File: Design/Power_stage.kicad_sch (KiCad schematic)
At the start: 4 parts, among them U3 CRE1S0505S3C, U6 CRE1S0505S3C

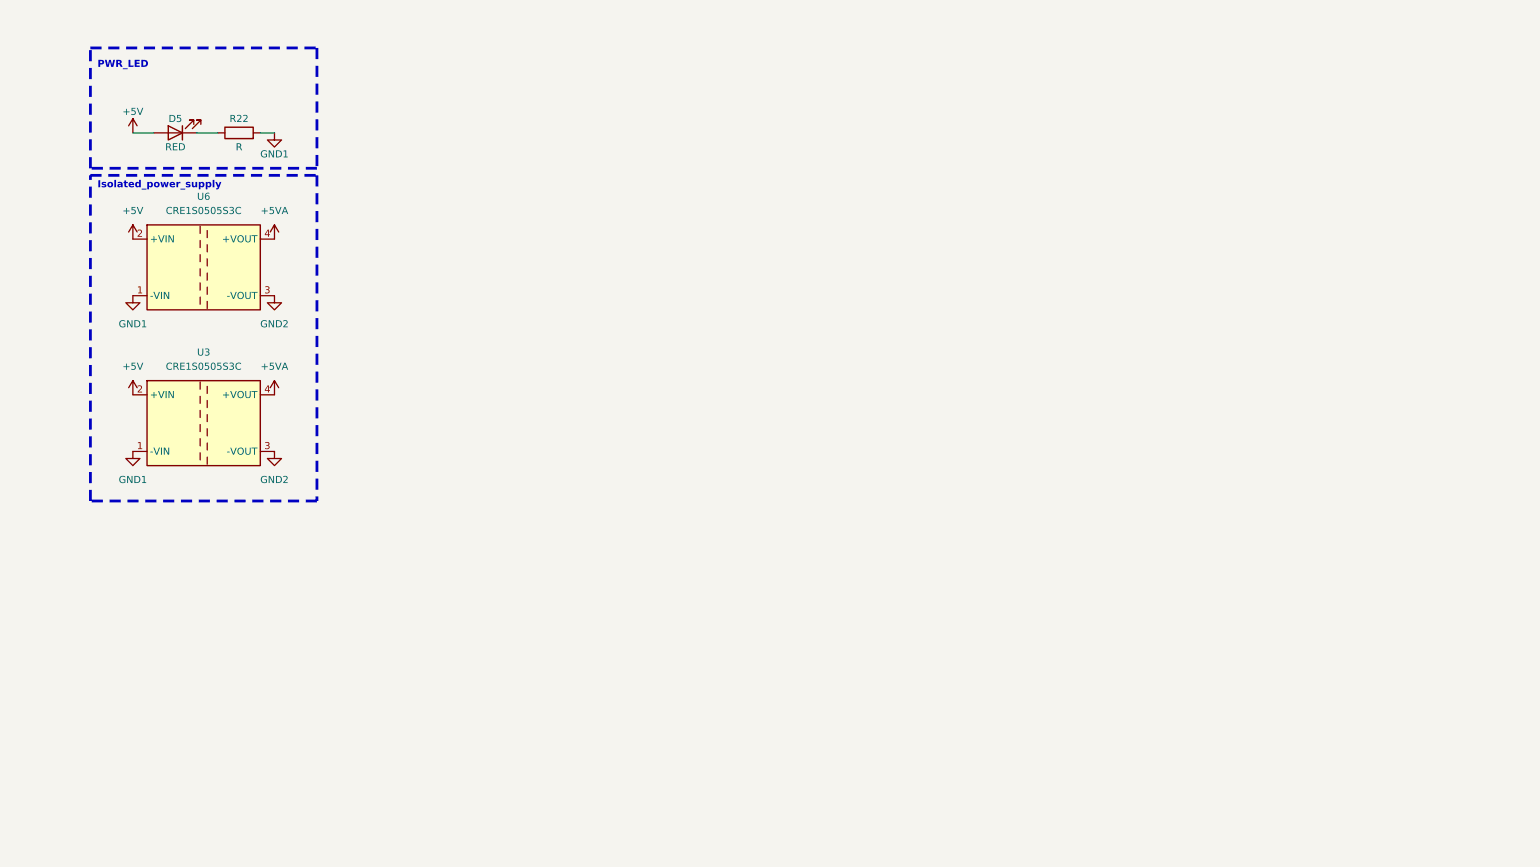
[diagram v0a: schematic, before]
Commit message: Setup Power supply
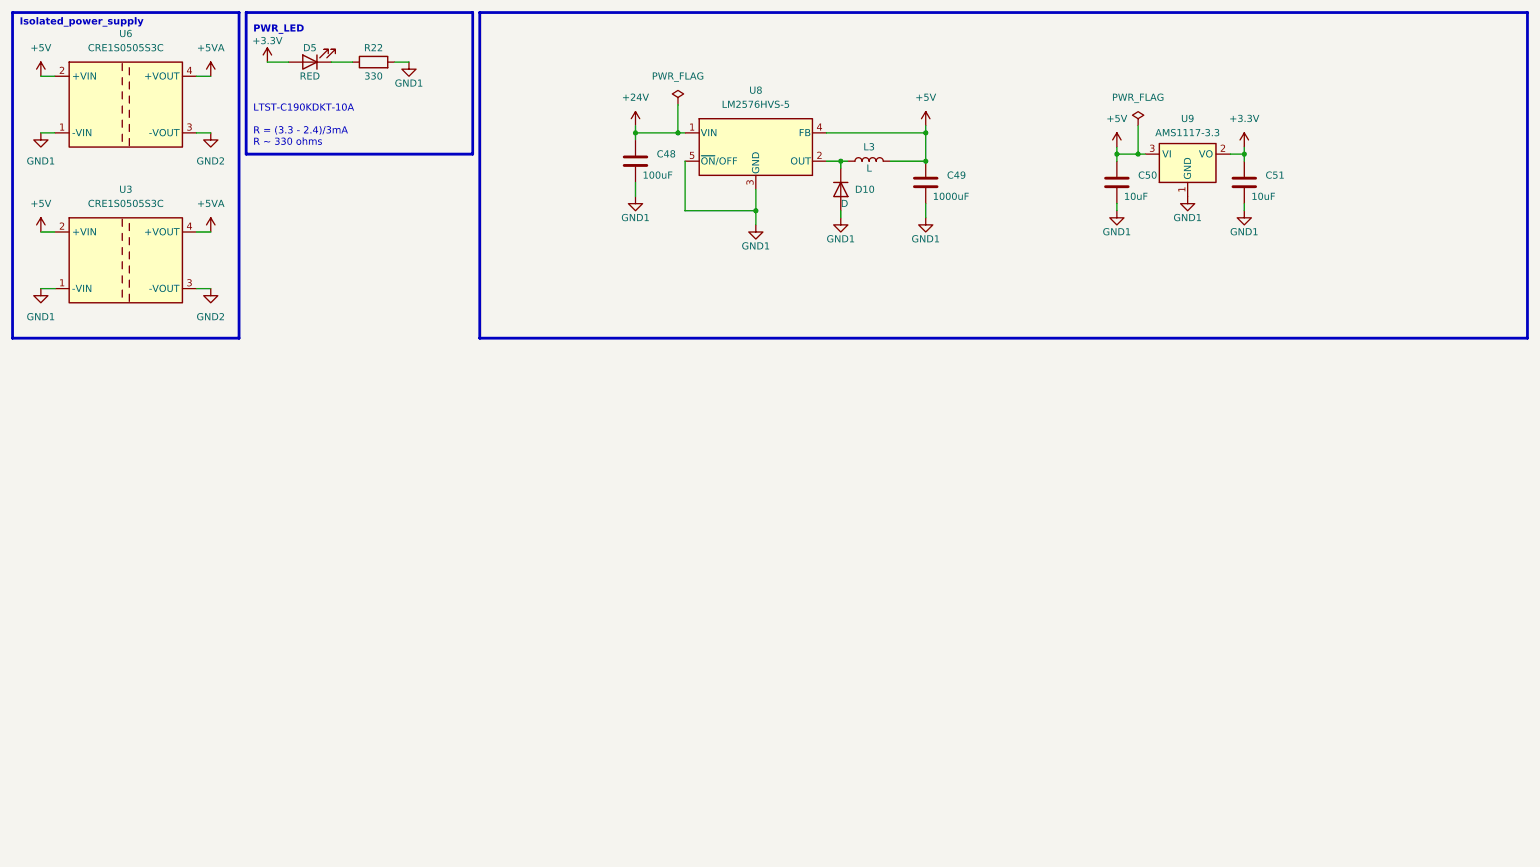
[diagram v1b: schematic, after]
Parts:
- added C48: 100uF, symbol Device:C
- added C49: 1000uF, symbol Device:C
- added C50, C51: 10uF, symbol Device:C
- added D10: D, symbol Device:D
- added L3: L, symbol Device:L
- added U8: LM2576HVS-5, Package_TO_SOT_SMD:TO-263-5_TabPin3, symbol Regulator_Switching:LM2576HVS-5
- added U9: AMS1117-3.3, Package_TO_SOT_SMD:SOT-223-3_TabPin2, symbol Regulator_Linear:AMS1117-3.3
- R22: value R -> 330
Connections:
- net +5V: now also C49.1, C50.1, L3.2, U8.4 (FB), U9.3 (VI); no longer D5.2 (A)
- net GND1: now also C48.2, C49.2, C50.2, C51.2, D10.2 (A), U8.3 (GND), U8.5 (~{ON}/OFF), U9.1 (GND)
- new net: D10.1 (K), L3.1, U8.2 (OUT)
- new net +24V: C48.1, U8.1 (VIN)
- new net +3.3V: C51.1, D5.2 (A), U9.2 (VO)
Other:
- note added: "LTST-C190KDKT-10A R = (3.3 - 2.4)/3mA R ~ 330 ohms"
- moved on the sheet: D5, R22, U3, U6

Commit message: Footprints added to all componenets
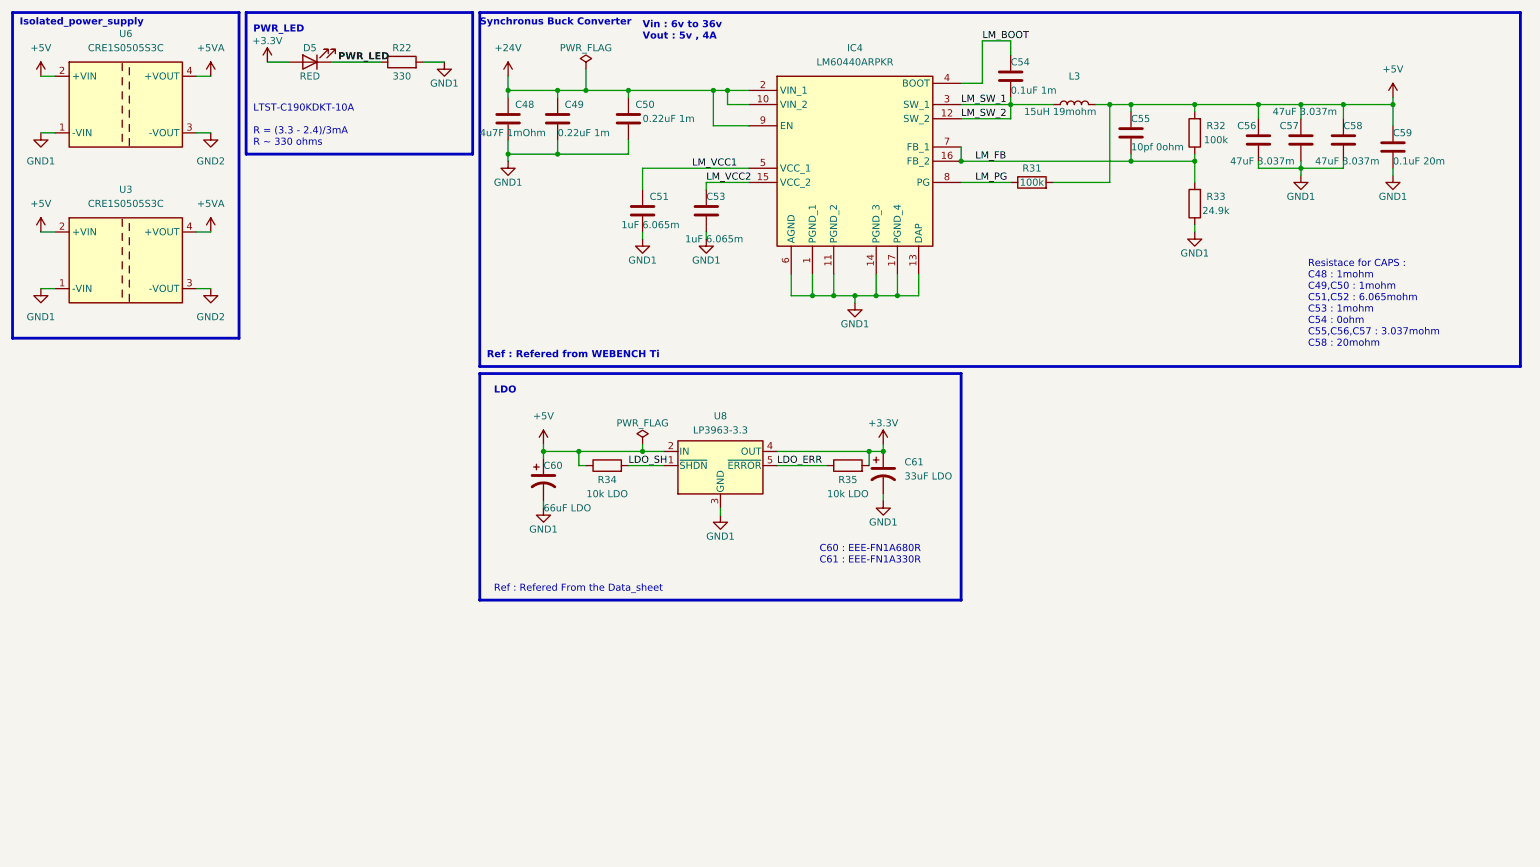
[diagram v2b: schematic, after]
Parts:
- removed D10: D, symbol Device:D
- removed U8: LM2576HVS-5, Package_TO_SOT_SMD:TO-263-5_TabPin3, symbol Regulator_Switching:LM2576HVS-5
- removed U9: AMS1117-3.3, Package_TO_SOT_SMD:SOT-223-3_TabPin2, symbol Regulator_Linear:AMS1117-3.3
- added C53: 1uF 6.065m, Capacitor_SMD:C_0603_1608Metric_Pad1.08x0.95mm_HandSolder, symbol Device:C
- added C54: 0.1uF 1m, Capacitor_SMD:C_0603_1608Metric_Pad1.08x0.95mm_HandSolder, symbol Device:C
- added C55: 10pf 0ohm, Capacitor_SMD:C_0805_2012Metric_Pad1.18x1.45mm_HandSolder, symbol Device:C
- added C56, C57, C58: 47uF 3.037m, Capacitor_SMD:C_0805_2012Metric_Pad1.18x1.45mm_HandSolder, symbol Device:C
- added C59: 0.1uF 20m, Capacitor_SMD:C_0603_1608Metric_Pad1.08x0.95mm_HandSolder, symbol Device:C
- added C60: 66uF LDO, Capacitor_SMD:CP_Elec_5x5.8, symbol Device:C_Polarized_US
- added C61: 33uF LDO, Capacitor_SMD:CP_Elec_4x5.8, symbol Device:C_Polarized_US
- added IC4: LM60440ARPKR, LM60440ARPKR_Buck:LM60440AQRPKRQ1, symbol LM60440ARPKR_Buck:LM60440ARPKR
- added R31, R32: 100k, Resistor_SMD:R_0805_2012Metric_Pad1.20x1.40mm_HandSolder, symbol Device:R
- added R33: 24.9k, Resistor_SMD:R_0805_2012Metric_Pad1.20x1.40mm_HandSolder, symbol Device:R
- added R34, R35: 10k LDO, Resistor_SMD:R_0805_2012Metric_Pad1.20x1.40mm_HandSolder, symbol Device:R
- added U8: LP3963-3.3, Package_TO_SOT_SMD:TO-263-5_TabPin3, symbol Regulator_Linear:LP3963-3.3
- C48: value 100uF -> 4u7F 1mOhm; footprint (none) -> Capacitor_SMD:C_0805_2012Metric_Pad1.18x1.45mm_HandSolder
- C49: value 1000uF -> 0.22uF 1m; footprint (none) -> Capacitor_SMD:C_0603_1608Metric_Pad1.08x0.95mm_HandSolder
- C50: value 10uF -> 0.22uF 1m; footprint (none) -> Capacitor_SMD:C_0603_1608Metric_Pad1.08x0.95mm_HandSolder
- C51: value 10uF -> 1uF 6.065m; footprint (none) -> Capacitor_SMD:C_0603_1608Metric_Pad1.08x0.95mm_HandSolder
- D5: footprint (none) -> LED_SMD:LED_0603_1608Metric_Pad1.05x0.95mm_HandSolder
- L3: value L -> 15uH 19mohm
- R22: footprint (none) -> Resistor_SMD:R_0603_1608Metric_Pad0.98x0.95mm_HandSolder
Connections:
- net +24V: now also C49.1, C50.1, IC4.10 (VIN_2), IC4.2 (VIN_1), IC4.9 (EN)
- net +3.3V: now also C61.1, R35.2, U8.4 (OUT); no longer C51.1
- net +5V: now also C55.1, C56.1, C57.1, C58.1, C59.1, C60.1, R31.2, R32.2, R34.1, U8.2 (IN); no longer C49.1, C50.1
- net GND1: now also C53.2, C56.2, C57.2, C58.2, C59.2, C60.2, C61.2, IC4.1 (PGND_1), IC4.11 (PGND_2), IC4.13 (DAP), IC4.14 (PGND_3), IC4.17 (PGND_4), IC4.6 (AGND), R33.1, U8.3 (GND)
- net PWR_LED: now reaches D5.1 (K), R22.1
- net LM_SW_1: now reaches L3.1
- net LM_SW_1: now also C54.2, IC4.12 (SW_2), IC4.3 (SW_1)
- new net LDO_ERR: R35.1, U8.5 (~{ERROR})
- new net LDO_SH: R34.2, U8.1 (~{SHDN})
- new net LM_BOOT: C54.1, IC4.4 (BOOT)
- new net LM_FB: C55.2, IC4.16 (FB_2), IC4.7 (FB_1), R32.1, R33.2
- new net LM_PG: IC4.8 (PG), R31.1
- new net LM_VCC1: C51.1, IC4.5 (VCC_1)
- new net LM_VCC2: C53.1, IC4.15 (VCC_2)
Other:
- note added: "C60 : EEE-FN1A680R C61 : EEE-FN1A330R"
- note added: "LDO"
- note added: "Ref : Refered From the Data_sheet"
- note added: "Ref : Refered from WEBENCH Ti"
- note added: "Resistace for CAPS : C48 : 1mohm C49,C50 : 1mohm C51,C52 : 6.065mohm C53 : 1mohm C54 : 0ohm C55,C56,C57 : 3.037mohm C58 : 20mohm"
- note added: "Synchronus Buck Converter"
- note added: "Vin : 6v to 36v Vout : 5v , 4A"
- moved on the sheet: R22

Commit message: CMC component name added
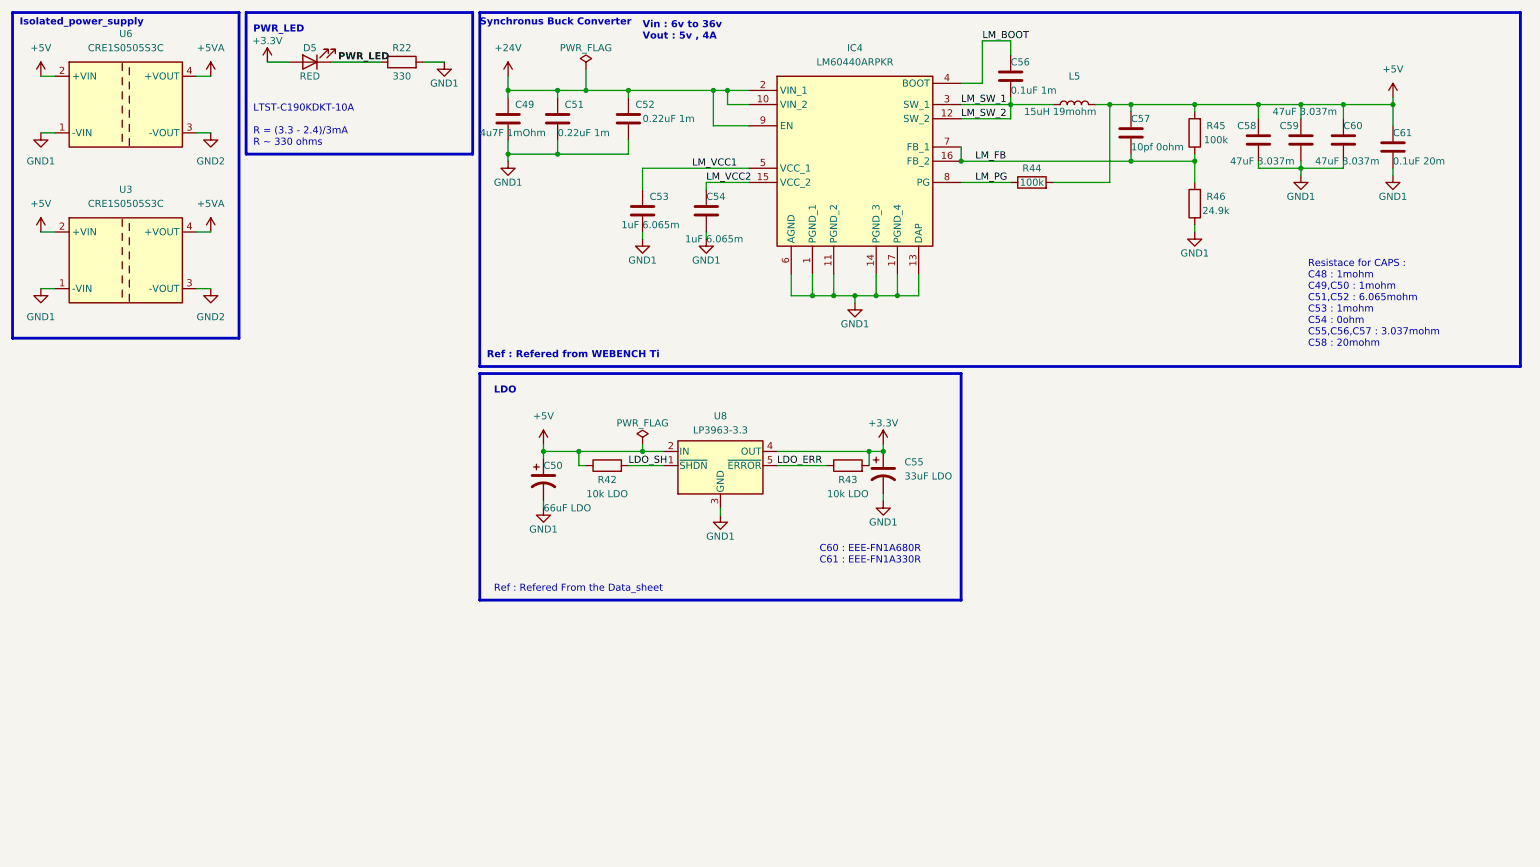
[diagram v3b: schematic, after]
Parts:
- renumbered C48 to C49, C60 to C50, C49 to C51, C50 to C52, C51 to C53, C53 to C54, C61 to C55, C54 to C56, C55 to C57, C56 to C58, C57 to C59, C58 to C60, C59 to C61, L3 to L5, R34 to R42, R35 to R43, R31 to R44, R32 to R45, R33 to R46

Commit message: Schematic Design complete
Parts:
- removed C61: 0.1uF 20m, Capacitor_SMD:C_0603_1608Metric_Pad1.08x0.95mm_HandSolder, symbol Device:C
- added J15: Input Power, TerminalBlock_Phoenix:TerminalBlock_Phoenix_MKDS-1,5-2_1x02_P5.00mm_Horizontal, symbol Connector:Screw_Terminal_01x02
- added TP1, TP10, TP11, TP12, TP13, TP14, TP2, TP3, TP4, TP5, TP6, TP7, TP8, TP9: TestPoint, TestPoint:TestPoint_Pad_D2.5mm, symbol Connector:TestPoint
- C57: value 10pf 0ohm -> 27pF 1mohm
- C58, C59: value 47uF 3.037m -> 100uF 1mohm
- C60: value 47uF 3.037m -> 100uF 30mohm
- L5: value 15uH 19mohm -> 8.2 24mohm; footprint (none) -> Inductor_SMD:L_Coilcraft_XAL6060-XXX
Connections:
- net +24V: now also J15.2 (Pin_2), TP2.1
- net +3.3V: now also TP4.1
- net +5V: now also TP3.1, TP5.1, TP9.1
- net +5VA: now also TP11.1, TP7.1
- net GND1: now also J15.1 (Pin_1), TP1.1, TP10.1, TP13.1, TP14.1, TP6.1
- net GND2: now also TP12.1, TP8.1
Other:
- note added: "L5 : XAL6060-822MEC"
- moved on the sheet: C50, C55, D5, R22, R42, R43, U3, U6, U8
